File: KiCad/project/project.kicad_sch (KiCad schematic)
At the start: 15 parts, among them P1 Header-Female-2.54_1x3, U1 DRV8313PWPR

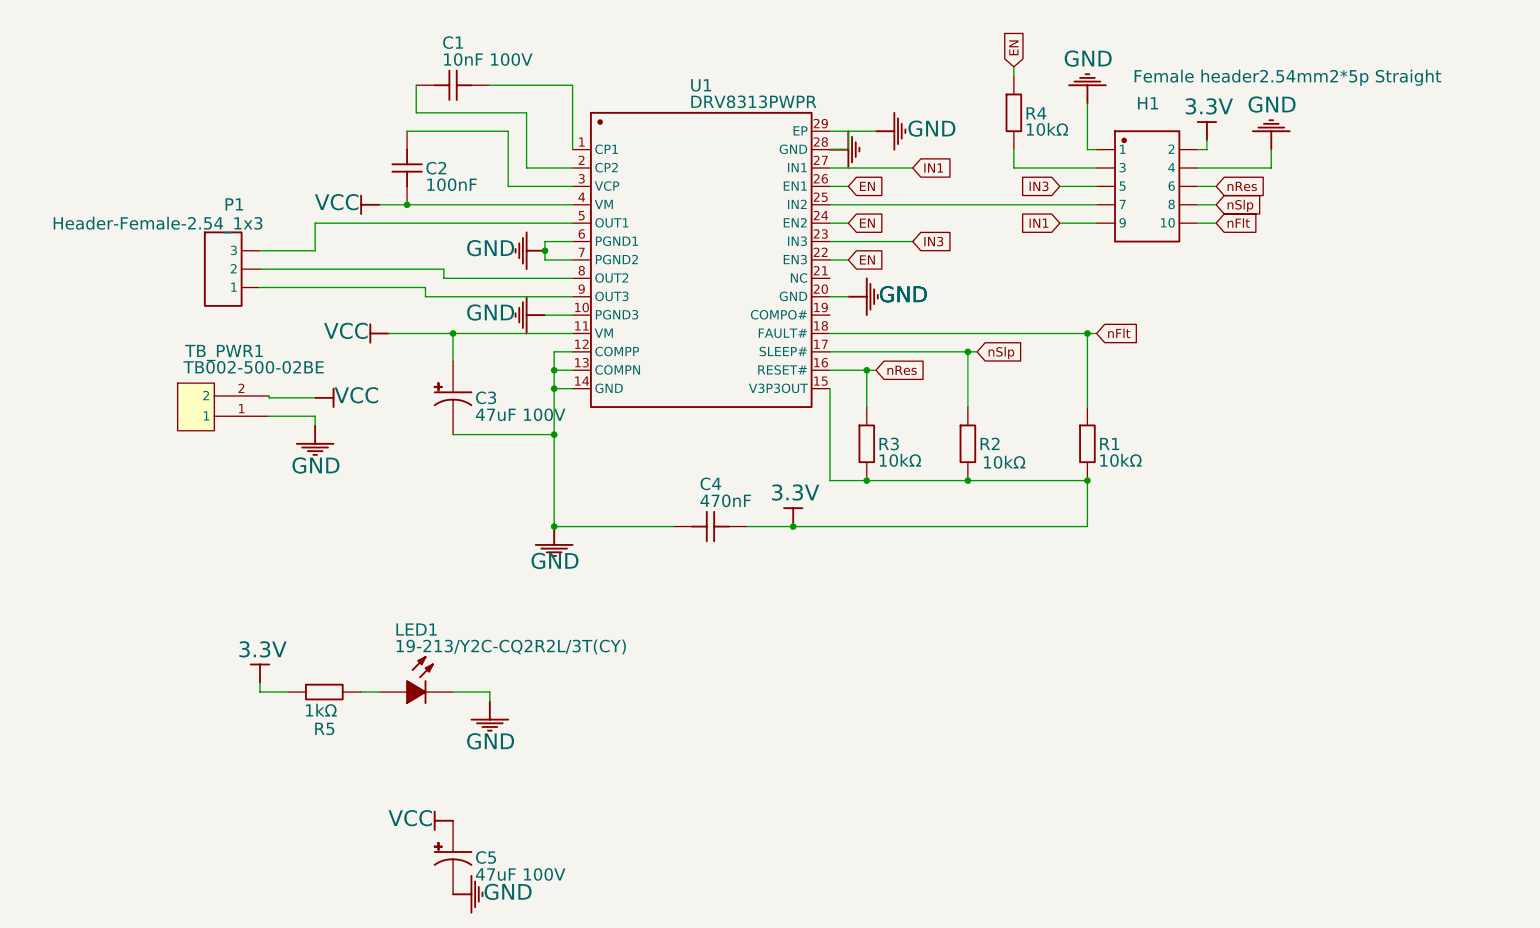
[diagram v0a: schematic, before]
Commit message: Schematic: brushed/solenoid + current-limit redesign (comparator, P1 5-pos, H1 2x7 EN breakout)
Done headless via kicad-skip; every new/changed net netlist-verified (kicad-cli).

Comparator current-sense network (TI DRV8313 Fig.12):
- PGND1/2/3 + COMPP split off GND onto a single shunt R8 (50mohm) -> GND.
- COMPN reference: divider R9(43k)/R10(62k)/R11(1k) with solder jumpers SJ1/SJ2
  (default 2.5A trip; cut SJ1->1.5A; cut SJ2->disabled) + filter cap C6 (0.47uF).
- nCOMPO pull-up R12 (10k) to 3V3.

P1 -> 5-pos terminal block [GND M1 M2 M3 VM] (lib-symbol extended to 5 pins);
M1/M2/M3 = OUT1/OUT2/OUT3, VM enables sensed low-side loads.

H1 -> 2x7: EN1/EN2/EN3 broken out, each via its own series 10k (R4/R6/R7) to its
header pin; comparator exposed (nCOMPO, COMPP=PGND sense, COMPN=VREF). Pinout:
GND 3V3 / IN1 EN1 / IN2 EN2 / IN3 EN3 / nRST nSLP / nFLT nCOMPO / COMPP COMPN.

Only U1.21 (NC) unconnected (correct). Remaining ERC items are pre-existing import
artifacts (lib_symbol_issues/pin_to_pin/power_pin_not_driven) plus cosmetic dangling
wire/label remnants from the connector swaps (no netlist impact; GUI tidy pending).

Co-Authored-By: Claude Opus 4.8 (1M context) <noreply@anthropic.com>
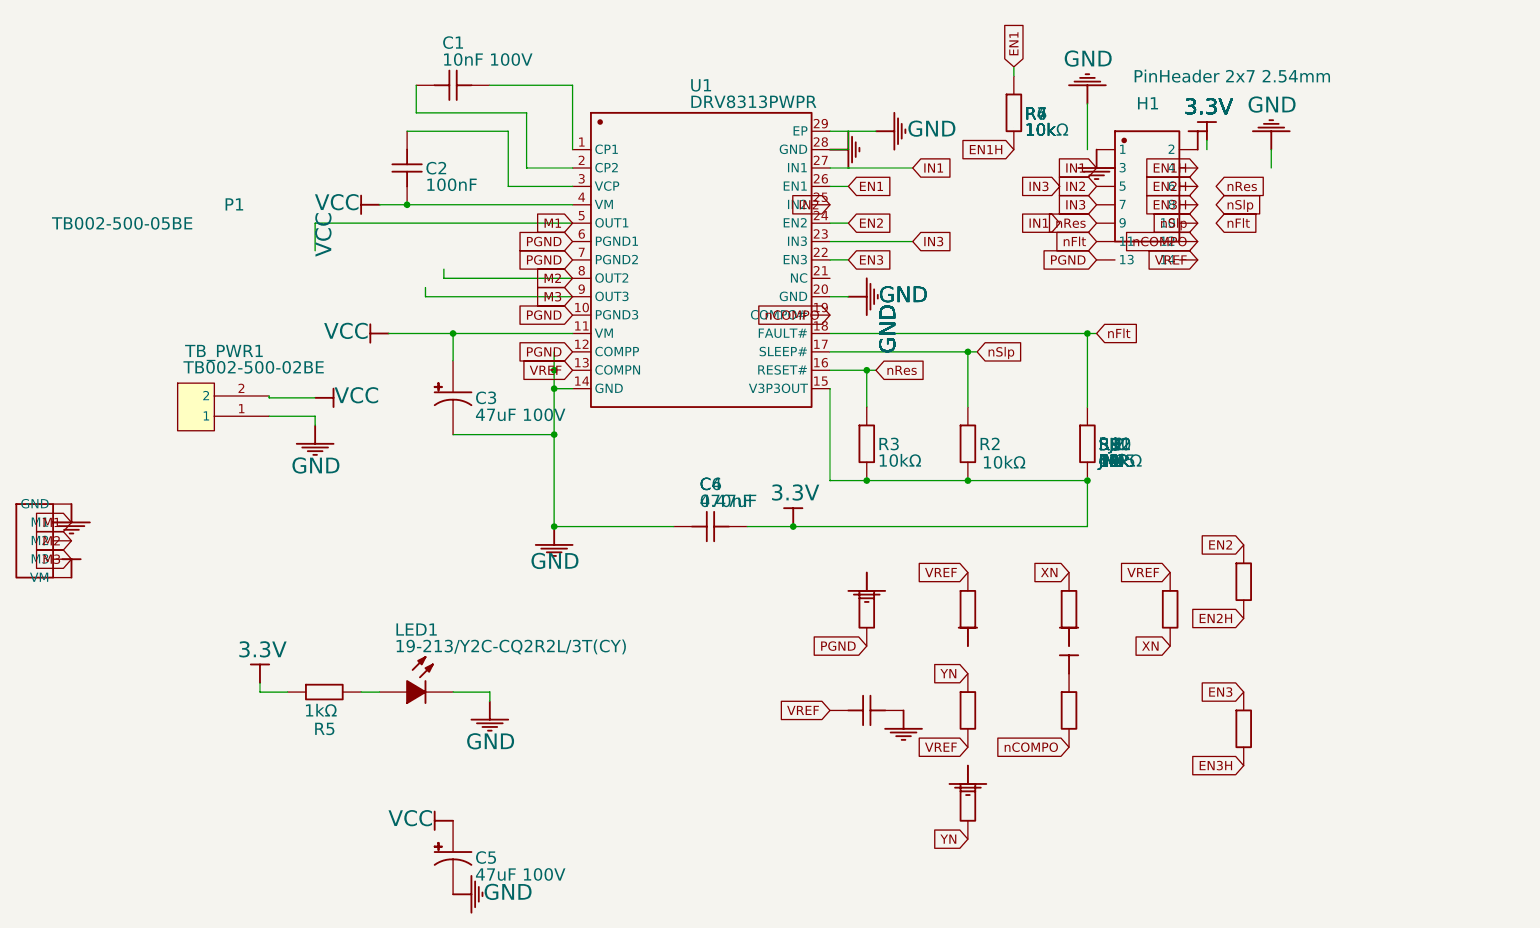
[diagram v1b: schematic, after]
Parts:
- added C6: 0.47uF, symbol CC0603ZRY5V6BB474
- added R10: 62k, symbol 0603WAF4701T5E_2
- added R11: 1k, symbol 0603WAF4701T5E_2
- added R12: 10k, symbol 0603WAF4701T5E_2
- added R6, R7: 10k, symbol 0603WAF4701T5E_3
- added R8: 0.05, symbol 0603WAF4701T5E_2
- added R9: 43k, symbol 0603WAF4701T5E_2
- added SJ1, SJ2: JMP, symbol 0603WAF4701T5E_2
- H1: value Female header2.54mm2*5p Straight -> PinHeader 2x7 2.54mm; Manufacturer ReliaPro -> (none); Manufacturer Part Female header2.54mm2*5p Straight -> (none); Supplier LCSC -> (none); Supplier Part C30419 -> (none)
- P1: value Header-Female-2.54_1x3 -> TB002-500-05BE
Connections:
- net 3.3V: now also R10.1, R12.2, R9.1
- net GND: now also P1.1 (GND), C6.2, R8.2, SJ2.2; no longer H1.4, U1.10 (PGND3), U1.12 (COMPP), U1.13 (COMPN), U1.6 (PGND1), U1.7 (PGND2)
- net IN1: now also H1.3; no longer H1.9
- net IN3: now also H1.7; no longer H1.5
- net VCC: now also P1.5 (VM)
- net nFlt: now also H1.11; no longer H1.10
- net nRes: now also H1.9; no longer H1.6
- net nSlp: now also H1.10; no longer H1.8
- net nCOMPO: now reaches U1.19 (COMPO#)
- net nCOMPO: now also H1.12, R12.1
- net IN2: now reaches U1.25 (IN2)
- net IN2: now also H1.5; no longer H1.7
- net M1: now reaches U1.5 (OUT1)
- net M1: now also P1.2 (M1); no longer P1.3
- net M2: now reaches U1.8 (OUT2)
- net M2: now also P1.3 (M2); no longer P1.2
- net M3: now reaches U1.9 (OUT3)
- net M3: now also P1.4 (M3); no longer P1.1
- net EN1H: now reaches R4.1
- net EN1H: now also H1.4; no longer H1.3
- net EN renamed EN1
- net EN1: no longer U1.22 (EN3), U1.24 (EN2)
- new net EN2: R6.2, U1.24 (EN2)
- new net EN2H: H1.6, R6.1
- new net EN3: R7.2, U1.22 (EN3)
- new net EN3H: H1.8, R7.1
- new net PGND: H1.13, R8.1, U1.10 (PGND3), U1.12 (COMPP), U1.6 (PGND1), U1.7 (PGND2)
- new net VREF: C6.1, H1.14, R11.1, R9.2, SJ1.2, U1.13 (COMPN)
- new net XN: R10.2, SJ1.1
- new net YN: R11.2, SJ2.1

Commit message: Footprints: back-annotate + library re-link (footprint_symbol_mismatch 29 -> 0)
Schematic Footprint fields were empty (footprints lived only in the PCB),
producing 29 footprint_symbol_mismatch parity items. Cleared all 29 headless
(pcbnew + kicad-skip); 0 unconnected, 0 error-severity DRC, 97 pads stable.

- 25x empty Footprint field, 2x stale PCB value text (C1 -> 10nF 100V,
  C3 -> 47uF 100V; PCB still read the v1.1 values), 2x SJ1/SJ2 BOM attr
  (excluded from BOM to match the SolderJumper footprint).
- Bare-name back-annotation alone just moves the problem to ERC (+25
  footprint_link_issues), since the embedded EasyEDA footprints have no
  library home. Fixed by giving them real lib:name homes on both sides:
  - 6 standard-origin footprints re-linked to canonical KiCad libs
    (Connector_PinSocket_2.54mm, TerminalBlock, Resistor_SMD, Jumper,
    MountingHole).
  - 5 EasyEDA footprints (C0603, R0603, LED0603-R-RD, CAP-SMD_BD6.3,
    HTSSOP-28) have no clean canonical match (geometry-verified) -> new
    project library KiCad/project/simplefocmini.pretty + project fp-lib-table.
- Result: footprint_symbol_mismatch 29 -> 0, ERC back to 141 baseline
  (footprint_link 25 -> 0). Re-linking surfaces 20 benign lib_footprint_mismatch
  FYIs (customized board footprints vs stock library) - left as-is.

Co-Authored-By: Claude Opus 4.8 (1M context) <noreply@anthropic.com>
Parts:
- C1, C2, C4, C6: footprint (none) -> simplefocmini:C0603
- C3, C5: footprint (none) -> simplefocmini:CAP-SMD_BD6.3-L6.6-W6.6-FD
- H1: footprint (none) -> Connector_PinSocket_2.54mm:PinSocket_2x07_P2.54mm_Vertical
- LED1: footprint (none) -> simplefocmini:LED0603-R-RD
- P1: footprint (none) -> TerminalBlock:TerminalBlock_MaiXu_MX126-5.0-05P_1x05_P5.00mm
- R1, R10, R11, R12, R2, R3, R4, R5, R6, R7, R9: footprint (none) -> simplefocmini:R0603
- R8: footprint (none) -> Resistor_SMD:R_2512_6332Metric
- SJ1, SJ2: footprint (none) -> Jumper:SolderJumper-2_P1.3mm_Bridged_RoundedPad1.0x1.5mm; now left out of the parts list
- TB_PWR1: footprint (none) -> TerminalBlock:TerminalBlock_MaiXu_MX126-5.0-02P_1x02_P5.00mm
- U1: footprint (none) -> simplefocmini:HTSSOP-28_L9.8-W4.5-P0.65-LS6.6-BL-EP

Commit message: PCB: re-place C3/C5 to the Ø10mm footprint (50x45 board); fixes part/footprint mismatch
C3/C5's BOM part C87862 (RVT2A470M1010, 47uF/100V) is a Ø10mm can but the
board had the Ø6.3mm footprint (surfaced by easyeda2kicad). Swapped to
CAP-SMD_BD10.0 and re-laid-out, headless. Electrically clean: 0 error-severity
DRC, 0 unconnected, all nets connected; schematic C3/C5 footprint synced.

- Enlarged 40x45 -> 50x45 (within the <=50x50 budget); relocated P1 + MH2/MH3
  to the new right edge (rest of the board untouched).
- Added CAP-SMD_BD10.0 to simplefocmini.pretty (from the easyeda2kicad download);
  swapped C3/C5 footprints (pad nets re-bound by name).
- Placed both cans rot90, stacked on the right, spread to clear the divider and
  the P1 fan; routed the phase/VM nets under the SMD cans on B.Cu. Autorouter was
  unstable on this congested area -> deterministic hand-route for the last mile.
- Re-poured In1/In2 GND planes to the new outline (inset to clear rounded corners).

Note: kicad-cli pcb drc normalises project.kicad_pro and resets the custom
min-via rules (0.4/0.25/0.075) -> false via violations; restored values, verified
clean with KiCadRoutingTools check_drc.py + check_connected.

Co-Authored-By: Claude Opus 4.8 (1M context) <noreply@anthropic.com>
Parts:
- C3, C5: footprint simplefocmini:CAP-SMD_BD6.3-L6.6-W6.6-FD -> simplefocmini:CAP-SMD_BD10.0-L10.3-W10.3-FD-LS11.0

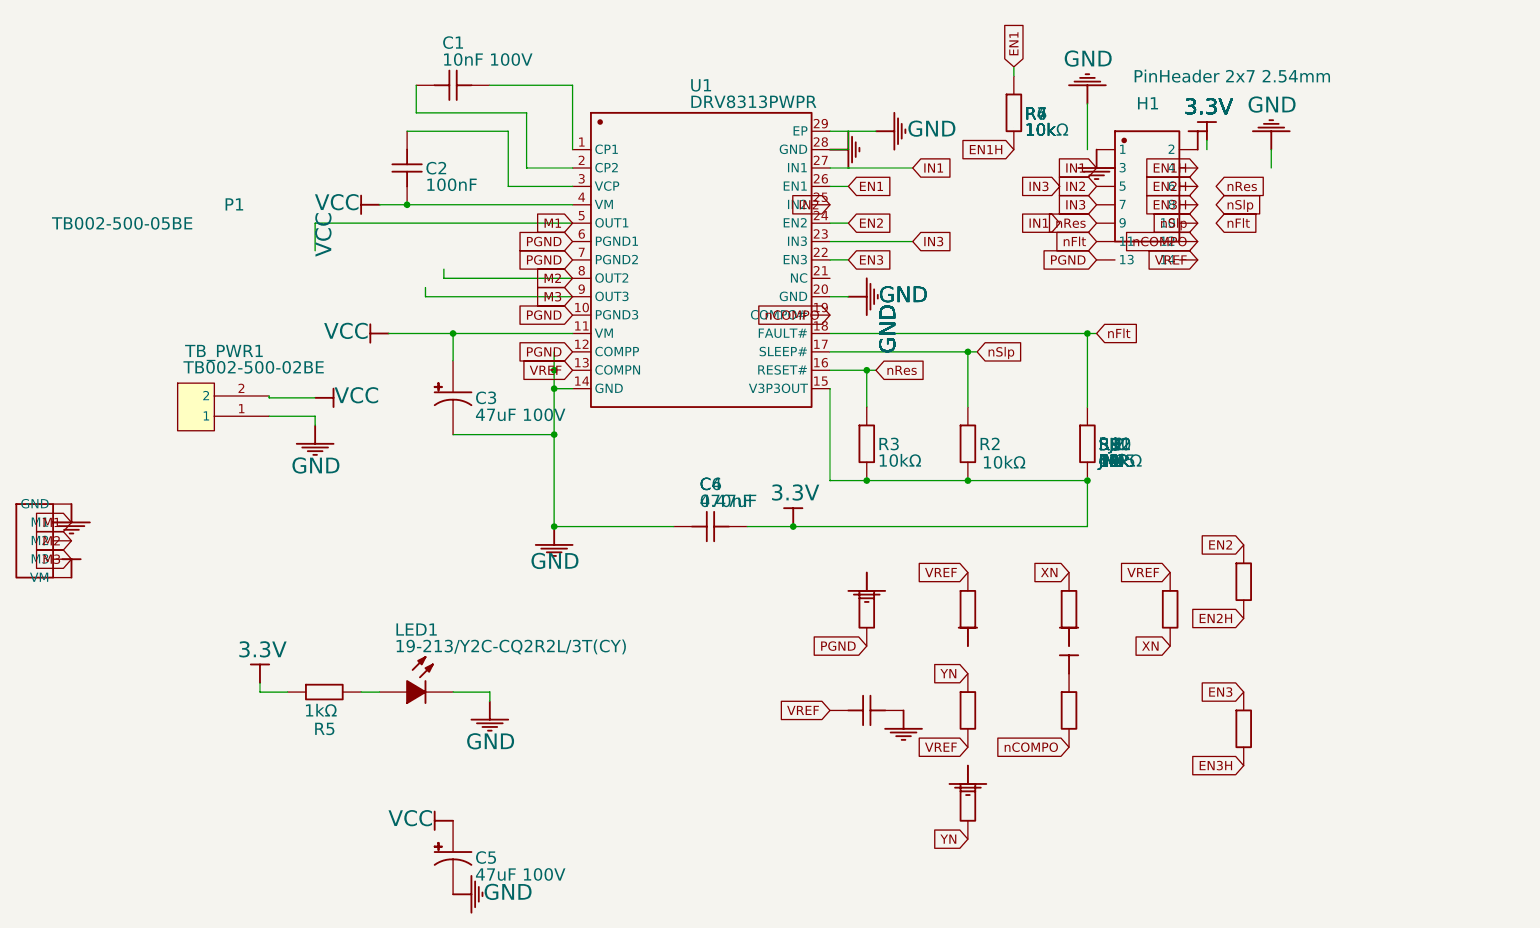
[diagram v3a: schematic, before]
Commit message: BOM: source all parts (JLCPCB Basic-preferred) + 3D models so all parts render
BOM (manufacturing/drv8313-board-BOM.csv) - fill every blank MPN/LCSC and fix
two import-era errors:
- R1-R4 carried the 4.7k part C23162 despite a 10k value -> C25804 (Basic)
- P1's C146243 was actually a 3-pin header, not the 5-pos block -> DB126V-5.0-5P (C2835160)
Filled: R6/R7/R12 10k C25804, R9 43k C23172, R10 62k C23221, R11 1k C21190,
R8 50mOhm 3W shunt C2903475, C6 470nF C1623 (= C4), H1 2x7 socket C38844,
TB_PWR1 2-pos block C395849. Values normalized so identical parts group;
PCB value text synced to match.

3D render - the project-local footprints referenced 3D models in directories
that were never committed (EASYEDA_MODELS / a deleted scratch dir), so U1, the
0603 passives, the LED and both cans dropped out of the render. Fetched the
exact models with easyeda2kicad into KiCad/project/EASYEDA_MODELS/ and repointed
every (model) to the committed .wrl. Terminal blocks (KiCad ships no 3D for the
MaiXu series here) got Degson DB126V models attached to the footprints.

Regenerated images/board-3d-{top,bottom}.png, images/schematic.svg and
manufacturing/drv8313-board.step (--subst-models). DRC 0 violations, all 27
nets connected, ERC at the 141 baseline. Docs updated (README, redesign-bom,
CLAUDE).

Co-Authored-By: Claude Opus 4.8 (1M context) <noreply@anthropic.com>
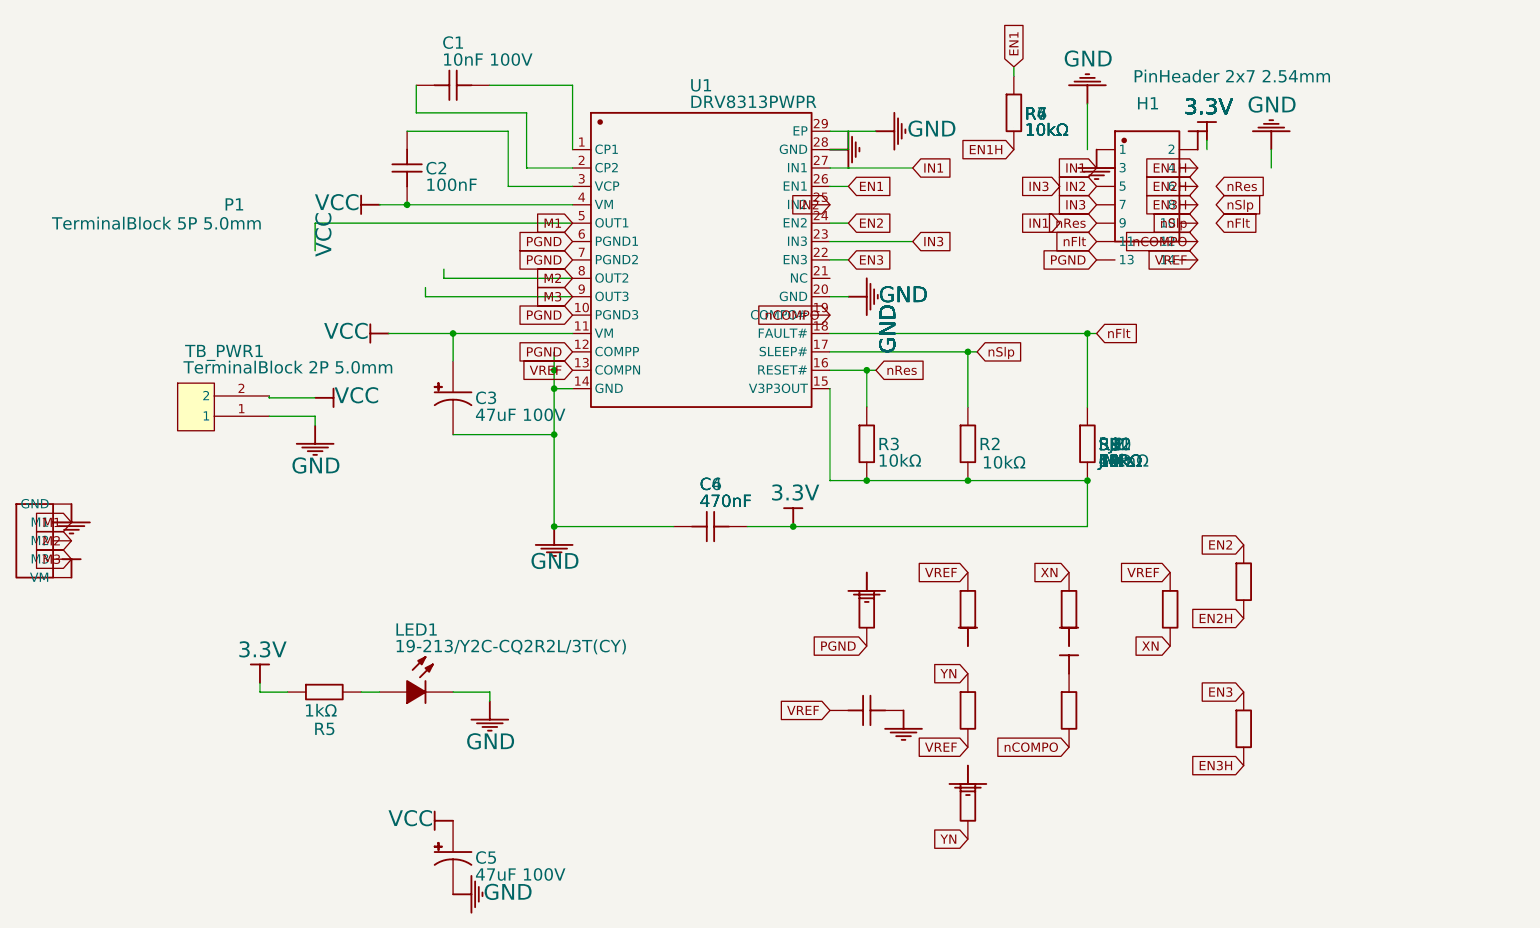
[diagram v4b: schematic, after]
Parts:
- C6: value 0.47uF -> 470nF; Manufacturer Part (none) -> CL10B474KA8NNNC; Supplier (none) -> LCSC; Supplier Part (none) -> C1623
- H1: Manufacturer Part (none) -> 2.54-2*7P Female; Supplier (none) -> LCSC; Supplier Part (none) -> C38844
- P1: value TB002-500-05BE -> TerminalBlock 5P 5.0mm; Manufacturer Part Header-Female-2.54_1x3 -> DB126V-5.0-5P-GN-P; Supplier Part C146243 -> C2835160
- R1, R2, R3, R4: Manufacturer Part 0603WAF4701T5E -> 0603WAF1002T5E; Supplier Part C23162 -> C25804
- R10: value 62k -> 62kΩ; Manufacturer Part (none) -> 0603WAF6202T5E; Supplier (none) -> LCSC; Supplier Part (none) -> C23221
- R11: value 1k -> 1kΩ; Manufacturer Part (none) -> 0603WAF1001T5E; Supplier (none) -> LCSC; Supplier Part (none) -> C21190
- R12, R6, R7: value 10k -> 10kΩ; Manufacturer Part (none) -> 0603WAF1002T5E; Supplier (none) -> LCSC; Supplier Part (none) -> C25804
- R8: value 0.05 -> 50mΩ; Manufacturer Part (none) -> HoJLR2512-3W-50mR-1%; Supplier (none) -> LCSC; Supplier Part (none) -> C2903475
- R9: value 43k -> 43kΩ; Manufacturer Part (none) -> 0603WAF4302T5E; Supplier (none) -> LCSC; Supplier Part (none) -> C23172
- TB_PWR1: value TB002-500-02BE -> TerminalBlock 2P 5.0mm; Manufacturer Part (none) -> DB126V-5.0-2P-GN-P; Supplier (none) -> LCSC; Supplier Part (none) -> C395849

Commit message: Tools: add JLCPCB part search + fab/silk scripts; re-source 2 BOM parts
Add tools/ headless helpers (see tools/README.md):
- jlc_search.py: live JLCPCB part finder. Ranks fee-free first (Basic OR
  Preferred -- both incur no per-part setup fee) then cheapest in-stock.
  Uses the API's server-side library filters (--fee-free/--basic/--preferred),
  which surface no-fee parts that plain keyword search buries behind Extended.
- build_manufacturing.py: regenerate gerbers/drill/zip/CPL/BOM/STEP + images
  in one command; snapshots/restores project.kicad_pro (kicad-cli rewrites it).
- set_silk_version.py: bump the vN.M (+ MM/YY) silkscreen stamp.

BOM cost/availability pass (jlc_search.py), non-geometric:
- C2 100nF C1591 (Extended) -> C14663 (YAGEO, Basic): drops a per-part fee;
  like-for-like 50V (netlist confirms C2 spans VCP-VM ~11V).
- LED1 C72038 (yellow, out of stock) -> C89811 (NationStar, yellow, Preferred,
  in stock) -- keeps original colour.
- Confirmed 43k/62k dividers are Preferred (fee-free), not Extended as earlier
  docs claimed; corrected README / redesign-bom / CLAUDE.md.
- Kept the unavoidable Extended parts (U1, 10nF/100V & 47uF/100V caps, 50mR
  shunt, connectors). 10k C25804 is Basic but read stock 0 -- flagged.

0 error-severity DRC, 27/27 nets connected, ERC 141 baseline (unchanged).

Co-Authored-By: Claude Opus 4.8 (1M context) <noreply@anthropic.com>
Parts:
- C2: Manufacturer Part CL10B104KB8NNNC -> CC0603KRX7R9BB104; Supplier Part C1591 -> C14663
- LED1: value 19-213/Y2C-CQ2R2L/3T(CY) -> Yellow; Manufacturer Part 19-213/Y2C-CQ2R2L/3T(CY) -> NCD0603Y2; Supplier Part C72038 -> C89811
